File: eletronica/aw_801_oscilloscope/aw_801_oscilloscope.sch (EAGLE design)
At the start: 27 parts, among them IC1 ATTINY2313, IC2 LM3940, IC3 MEGA8-P, Q1 12Mhz, Q2 16Mhz, X1 USB, X2 USB

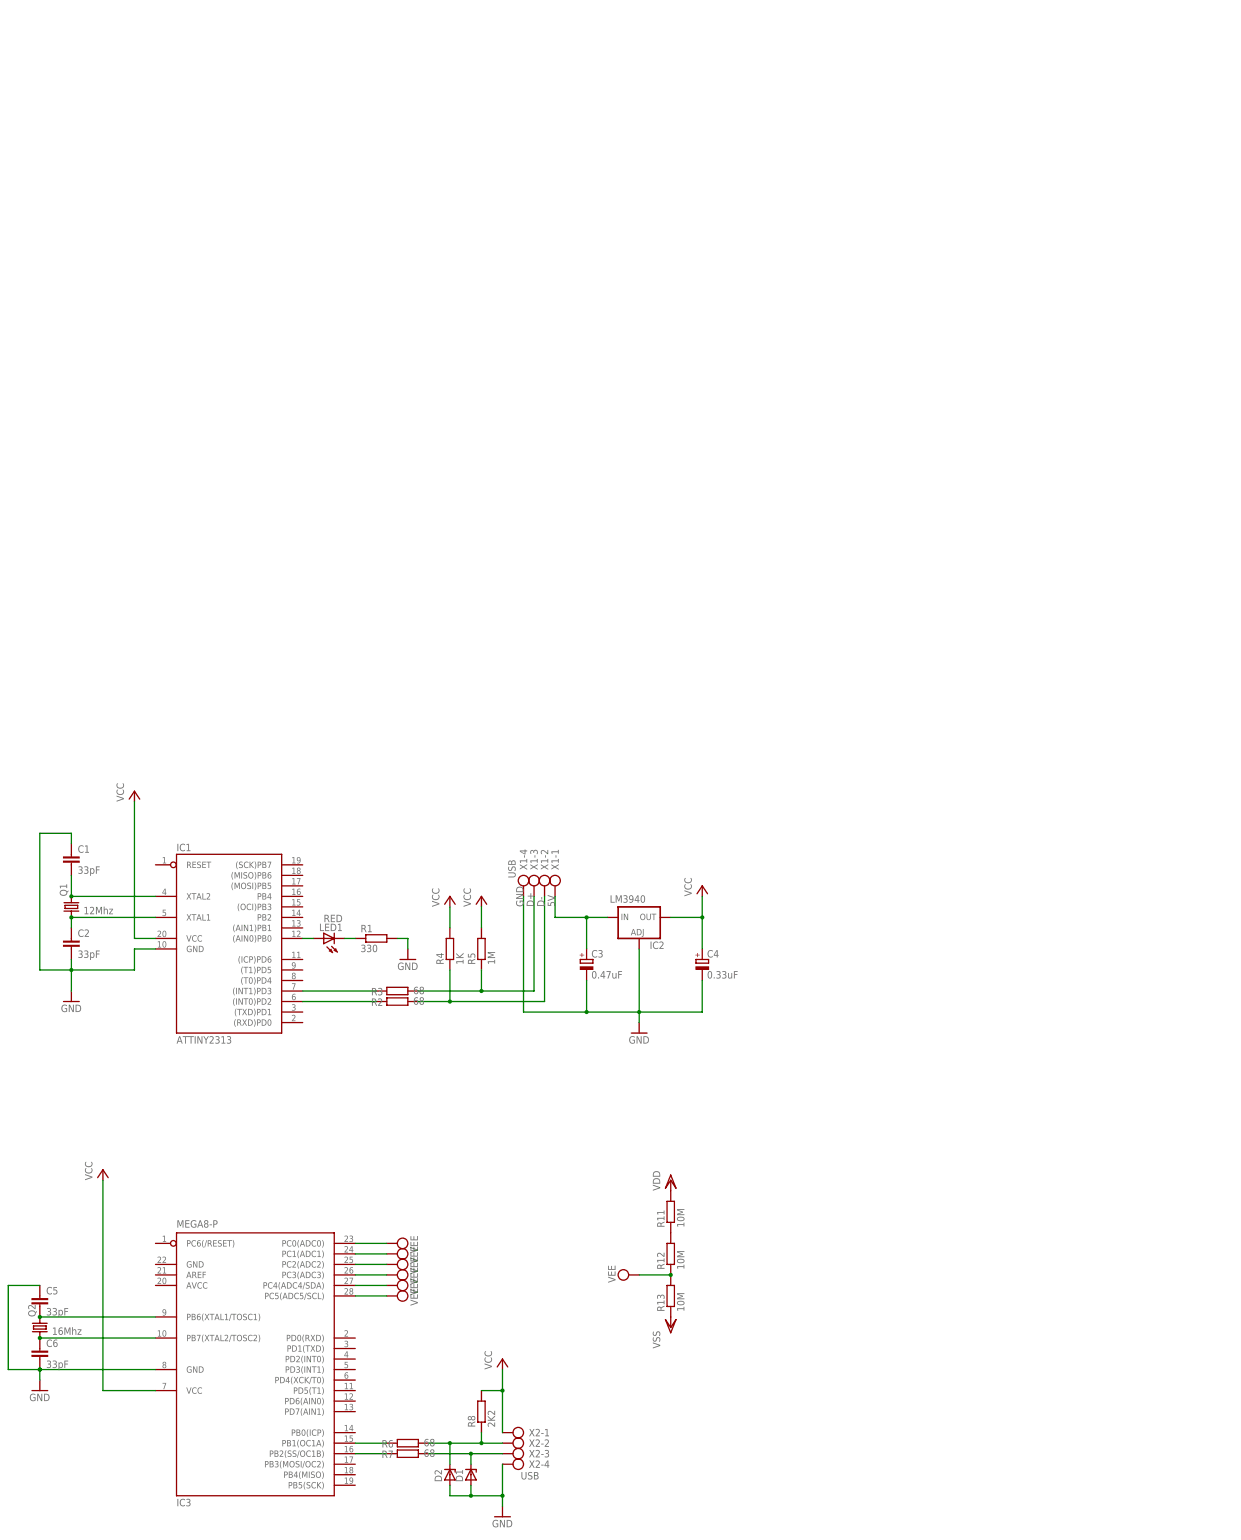
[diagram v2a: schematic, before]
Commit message: 
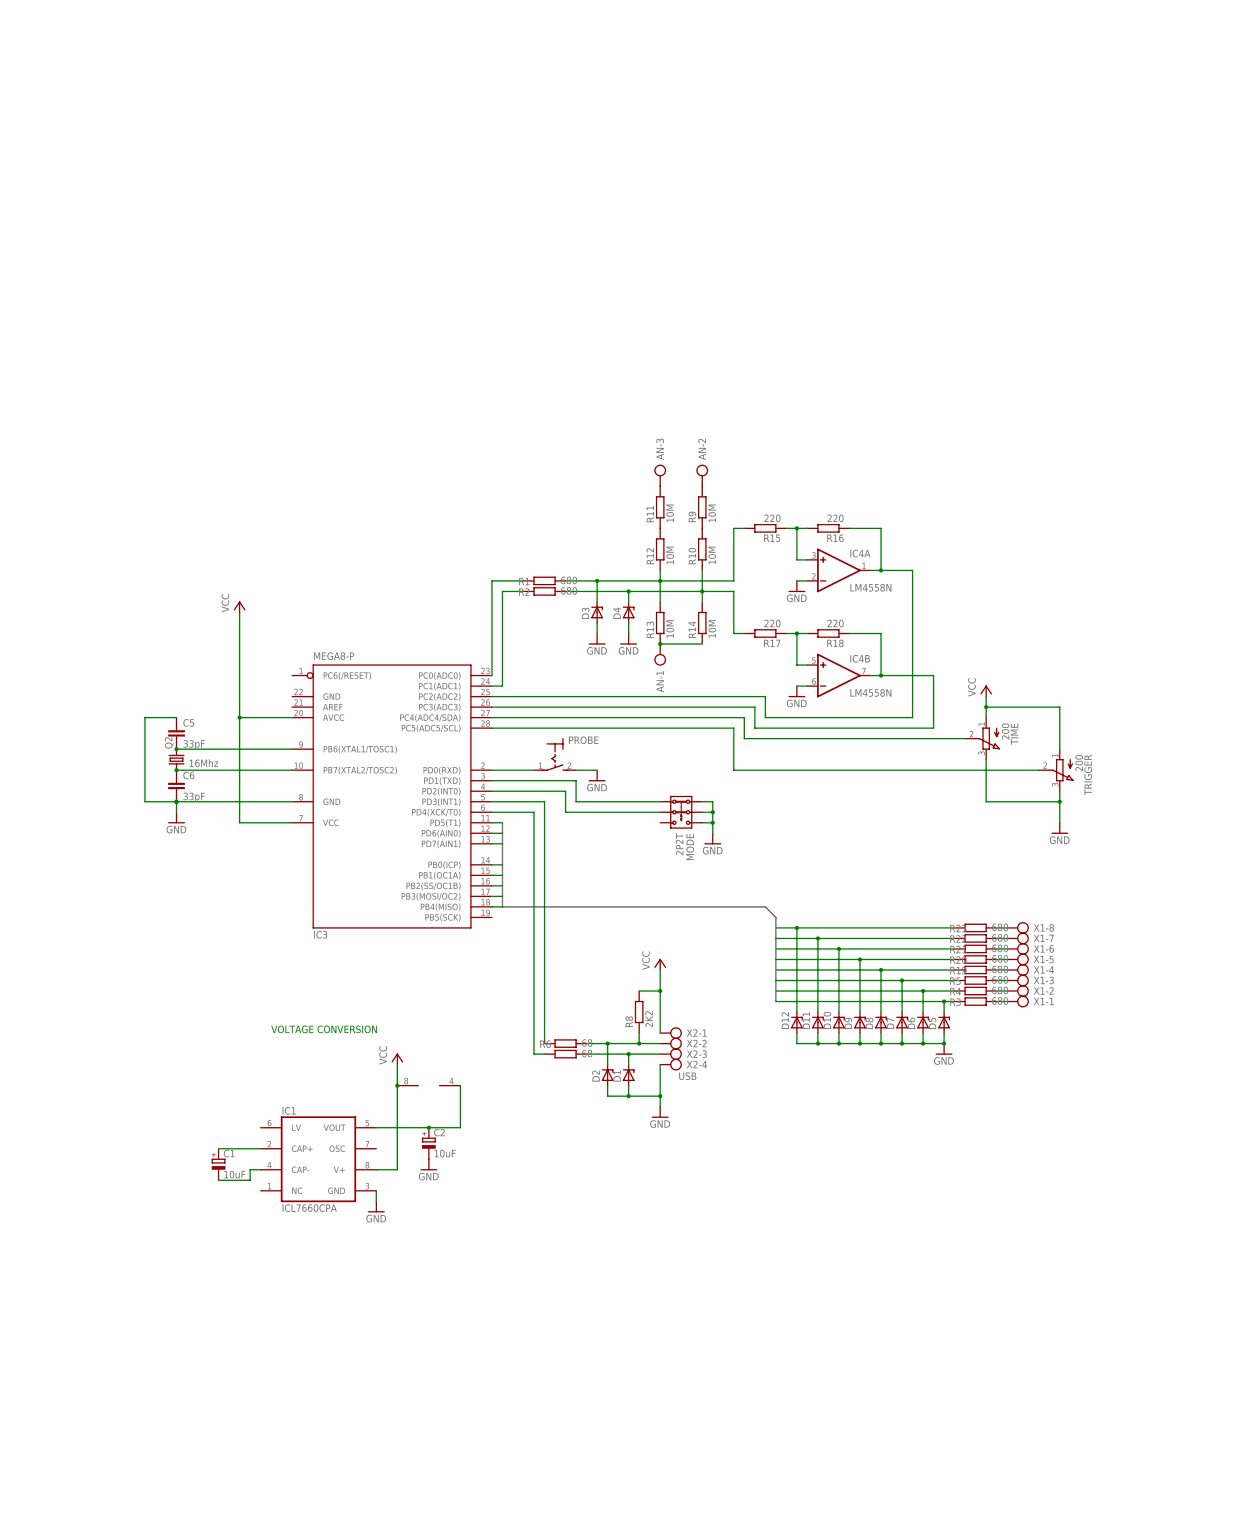
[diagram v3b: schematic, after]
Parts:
- removed C3: 0.47uF, rcl:CPOL-EUE2.5-6
- removed C4: 0.33uF, rcl:CPOL-EUE2.5-6
- removed IC2: LM3940, v-reg:LM317TS
- removed LED1: RED, led:LED5MM
- removed Q1: 12Mhz, crystal:CRYSTALHC49U70
- added AN: (no value), con-ptr500:AK500/3
- added D10, D11, D12, D3, D4, D5, D6, D7, D8, D9: (no value), diode:ZENER-DIODEDO35Z10
- added IC4: LM4558N, linear:LM4558N
- added MODE: 2P2T, switch:2P2T
- added PROBE: (no value), switch:MS243
- added R10, R14, R9: 10M, rcl:R-EU_0207/10
- added R15, R16, R17, R18: 220, rcl:R-EU_0207/10
- added R19, R20, R21, R22, R23: 680, rcl:R-EU_0207/10
- added TIME, TRIGGER: 200, pot:3RP/1610N
- C1, C2: value 33pF -> 10uF; device rcl:C-EU050-030X075 -> rcl:CPOL-EUE2.5-6
- IC1: value ATTINY2313 -> ICL7660CPA; device atmel:AT90S2313P -> maxim:ICL7660CPA
- R1: value 330 -> 680
- R2, R3: value 68 -> 680
- R4: value 1K -> 680
- R5: value 1M -> 680
- X1: value USB -> (none); device con-ptr500:AK500/4 -> con-ptr500:AK500/8
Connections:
- removed net 5V: C3.+, IC2.IN, X1-1.KL
- removed net D+: R3.2, R5.1, X1-3.KL
- removed net D-: R2.2, R4.1, X1-2.KL
- removed net VDD: R11.2
- removed net VEE: IC3.PC0(ADC0), IC3.PC1(ADC1), IC3.PC2(ADC2), IC3.PC3(ADC3), IC3.PC4(ADC4/SDA), IC3.PC5(ADC5/SCL), R12.1, R13.2
- removed net VSS: R13.1
- new net DIG0: D12.C, IC3.PD5(T1), R23.1
- new net DIG1: D11.C, IC3.PD6(AIN0), R22.1
- new net DIG2: D10.C, IC3.PD7(AIN1), R21.1
- new net DIG3: D9.C, IC3.PB0(ICP), R20.1
- new net DIG4: D8.C, IC3.PB1(OC1A), R19.1
- new net DIG5: D7.C, IC3.PB2(SS/OC1B), R5.1
- new net DIG6: D6.C, IC3.PB3(MOSI/OC2), R4.1
- new net DIG7: D5.C, IC3.PB4(MISO), R3.1
- new net N$13: AN-3.KL, R11.2
- new net N$14: R10.2, R9.1
- new net N$16: D4.C, R10.1, R14.2, R17.2, R2.2
- new net N$17: IC4A.+IN, R15.1, R16.2
- new net N$18: IC3.PC2(ADC2), IC4A.OUT, R16.1
- new net N$19: IC4B.+IN, R17.1, R18.2
- new net N$20: IC3.PC3(ADC3), IC4B.OUT, R18.1
- new net N$21: AN-2.KL, R9.2
- new net N$22: IC3.PC4(ADC4/SDA), TIME.S
- new net N$23: IC3.PC5(ADC5/SCL), TRIGGER.S
- new net N$24: AN-1.KL, R13.1, R14.1
- new net N$25: R23.2, X1-8.KL
- new net N$26: R22.2, X1-7.KL
- new net N$27: R21.2, X1-6.KL
- new net N$28: R20.2, X1-5.KL
- new net N$29: R19.2, X1-4.KL
- new net N$30: R5.2, X1-3.KL
- new net N$31: R4.2, X1-2.KL
- new net N$32: R3.2, X1-1.KL
- new net N$33: IC3.PC1(ADC1), R2.1
- new net N$34: IC3.PC0(ADC0), R1.1
- new net VOUT: C2.+, IC1.VOUT, IC4P.V-
- net GND: now also C2.-, D10.A, D11.A, D12.A, D3.A, D4.A, D5.A, D6.A, D7.A, D8.A, D9.A, IC4A.-IN, IC4B.-IN, MODE.1.1, MODE.2.1, MODE.3.1, PROBE.S, TIME.E, TRIGGER.E; no longer C1.1, C2.2, C3.-, C4.-, IC2.ADJ, R1.2, X1-4.KL
- net N$1: now also D3.C, R1.2, R12.1, R13.2, R15.2; no longer C1.2, IC1.XTAL2, Q1.2
- net N$11: now also IC3.PD3(INT1); no longer IC3.PB1(OC1A)
- net N$12: now also IC3.PD4(XCK/T0); no longer IC3.PB2(SS/OC1B)
- net N$2: now also C1.-, IC1.CAP-; no longer C2.1, IC1.XTAL1, Q1.1
- net N$3: now also C1.+, IC1.CAP+; no longer IC1.(AIN0)PB0, LED1.A
- net N$4: now also IC3.PD0(RXD), PROBE.P; no longer LED1.C, R1.1
- net N$5: now also IC3.PD1(TXD), MODE.1.2; no longer IC1.(INT0)PD2, R2.1
- net N$6: now also IC3.PD2(INT0), MODE.2.2; no longer IC1.(INT1)PD3, R3.1
- net VCC: now also IC1.V+, IC3.AVCC, IC4P.V+, TIME.A, TRIGGER.A; no longer C4.+, IC1.VCC, IC2.OUT, R4.2, R5.2
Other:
- note added: "VOLTAGE CONVERSION"
- moved on the sheet: C5, C6, D1, D2, IC3, Q2, R1, R11, R12, R13, R2, R3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

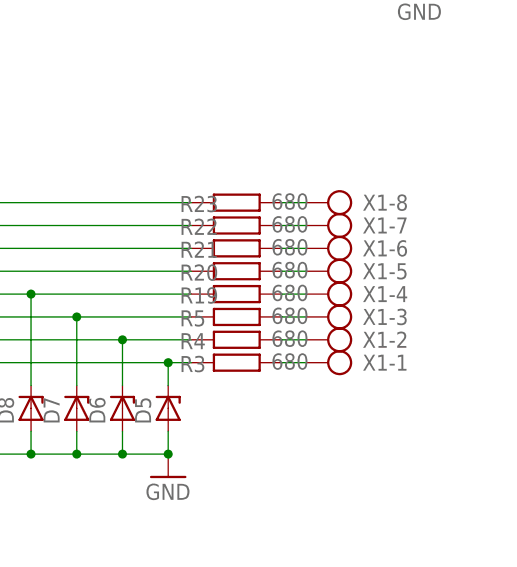
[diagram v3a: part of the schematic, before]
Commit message: 
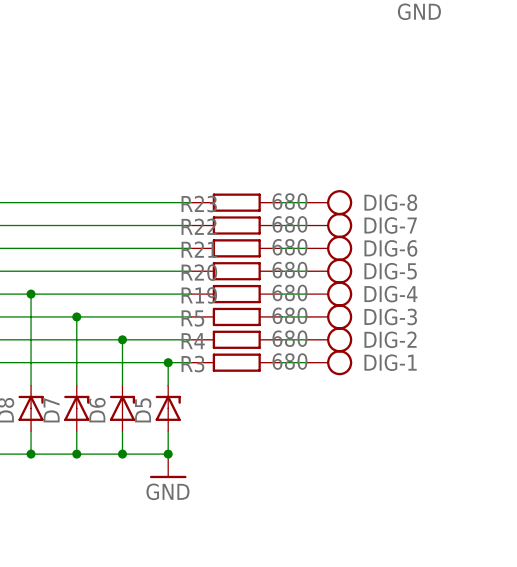
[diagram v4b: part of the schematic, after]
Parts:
- renumbered X1 to DIG
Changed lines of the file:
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@@
 <part name="GND10" library="supply1" deviceset="GND" device=""/>
 <part name="GND11" library="supply1" deviceset="GND" device=""/>
-<part name="X1" library="con-ptr500" deviceset="AK500/8" device=""/>
+<part name="DIG" library="con-ptr500" deviceset="AK500/8" device=""/>
 <part name="R3" library="rcl" deviceset="R-EU_" device="0207/10" value="680"/>
 <part name="R4" library="rcl" deviceset="R-EU_" device="0207/10" value="680"/>
@@
 <instance part="GND10" gate="1" x="127" y="147.32"/>
 <instance part="GND11" gate="1" x="134.62" y="147.32"/>
-<instance part="X1" gate="-1" x="231.14" y="60.96" rot="R180"/>
-<instance part="X1" gate="-2" x="231.14" y="63.5" rot="R180"/>
-<instance part="X1" gate="-3" x="231.14" y="66.04" rot="R180"/>
-<instance part="X1" gate="-4" x="231.14" y="68.58" rot="R180"/>
-<instance part="X1" gate="-5" x="231.14" y="71.12" rot="R180"/>
-<instance part="X1" gate="-6" x="231.14" y="73.66" rot="R180"/>
-<instance part="X1" gate="-7" x="231.14" y="76.2" rot="R180"/>
-<instance part="X1" gate="-8" x="231.14" y="78.74" rot="R180"/>
+<instance part="DIG" gate="-1" x="231.14" y="60.96" rot="R180"/>
+<instance part="DIG" gate="-2" x="231.14" y="63.5" rot="R180"/>
+<instance part="DIG" gate="-3" x="231.14" y="66.04" rot="R180"/>
+<instance part="DIG" gate="-4" x="231.14" y="68.58" rot="R180"/>
+<instance part="DIG" gate="-5" x="231.14" y="71.12" rot="R180"/>
+<instance part="DIG" gate="-6" x="231.14" y="73.66" rot="R180"/>
+<instance part="DIG" gate="-7" x="231.14" y="76.2" rot="R180"/>
+<instance part="DIG" gate="-8" x="231.14" y="78.74" rot="R180"/>
 <instance part="R3" gate="G$1" x="218.44" y="60.96" smashed="yes">
 <attribute name="NAME" x="212.09" y="59.9186" size="1.778" layer="95"/>
@@
 <segment>
 <pinref part="R23" gate="G$1" pin="2"/>
-<pinref part="X1" gate="-8" pin="KL"/>
+<pinref part="DIG" gate="-8" pin="KL"/>
 <wire x1="223.52" y1="78.74" x2="226.06" y2="78.74" width="0.1524" layer="91"/>
 </segment>
@@
 <segment>
 <pinref part="R22" gate="G$1" pin="2"/>
-<pinref part="X1" gate="-7" pin="KL"/>
+<pinref part="DIG" gate="-7" pin="KL"/>
 <wire x1="223.52" y1="76.2" x2="226.06" y2="76.2" width="0.1524" layer="91"/>
 </segment>
@@
 <segment>
 <pinref part="R21" gate="G$1" pin="2"/>
-<pinref part="X1" gate="-6" pin="KL"/>
+<pinref part="DIG" gate="-6" pin="KL"/>
 <wire x1="223.52" y1="73.66" x2="226.06" y2="73.66" width="0.1524" layer="91"/>
 </segment>
@@
 <segment>
 <pinref part="R20" gate="G$1" pin="2"/>
-<pinref part="X1" gate="-5" pin="KL"/>
+<pinref part="DIG" gate="-5" pin="KL"/>
 <wire x1="223.52" y1="71.12" x2="226.06" y2="71.12" width="0.1524" layer="91"/>
 </segment>
@@
 <segment>
 <pinref part="R19" gate="G$1" pin="2"/>
-<pinref part="X1" gate="-4" pin="KL"/>
+<pinref part="DIG" gate="-4" pin="KL"/>
 <wire x1="223.52" y1="68.58" x2="226.06" y2="68.58" width="0.1524" layer="91"/>
 </segment>
@@
 <segment>
 <pinref part="R5" gate="G$1" pin="2"/>
-<pinref part="X1" gate="-3" pin="KL"/>
+<pinref part="DIG" gate="-3" pin="KL"/>
 <wire x1="223.52" y1="66.04" x2="226.06" y2="66.04" width="0.1524" layer="91"/>
 </segment>
@@
 <segment>
 <pinref part="R4" gate="G$1" pin="2"/>
-<pinref part="X1" gate="-2" pin="KL"/>
+<pinref part="DIG" gate="-2" pin="KL"/>
 <wire x1="223.52" y1="63.5" x2="226.06" y2="63.5" width="0.1524" layer="91"/>
 </segment>
@@
 <segment>
 <pinref part="R3" gate="G$1" pin="2"/>
-<pinref part="X1" gate="-1" pin="KL"/>
+<pinref part="DIG" gate="-1" pin="KL"/>
 <wire x1="223.52" y1="60.96" x2="226.06" y2="60.96" width="0.1524" layer="91"/>
 </segment>
